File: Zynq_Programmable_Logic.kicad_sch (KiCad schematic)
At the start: 7 parts, among them Q100 T2N7002AK,LM, U1 XC7Z010-2CLG400I

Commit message: Added page '[7] 1GB DDR3L Modules'
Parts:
- renumbered D101 to D500, Q100 to Q500, R127 to R500, R104 to R501, R103 to R502, R123 to R503, U1 to U200
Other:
- company: (none) -> Designed By: Dylan Gutierrez

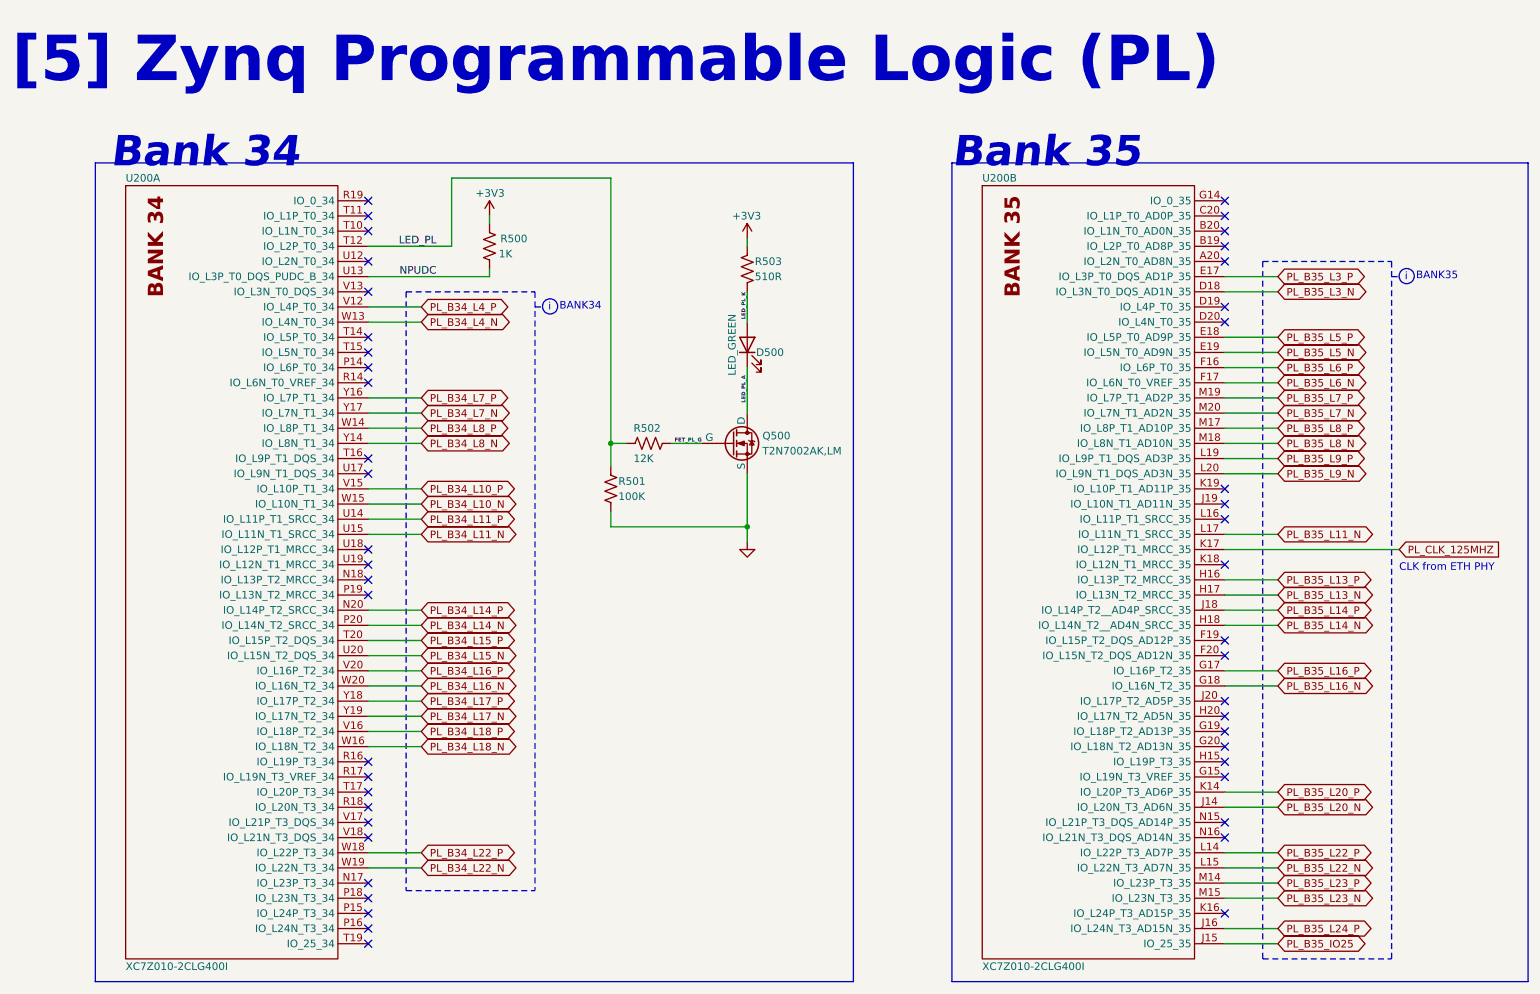
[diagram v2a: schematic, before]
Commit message: Finished first pass of schematic, needs netclass assignments and double check
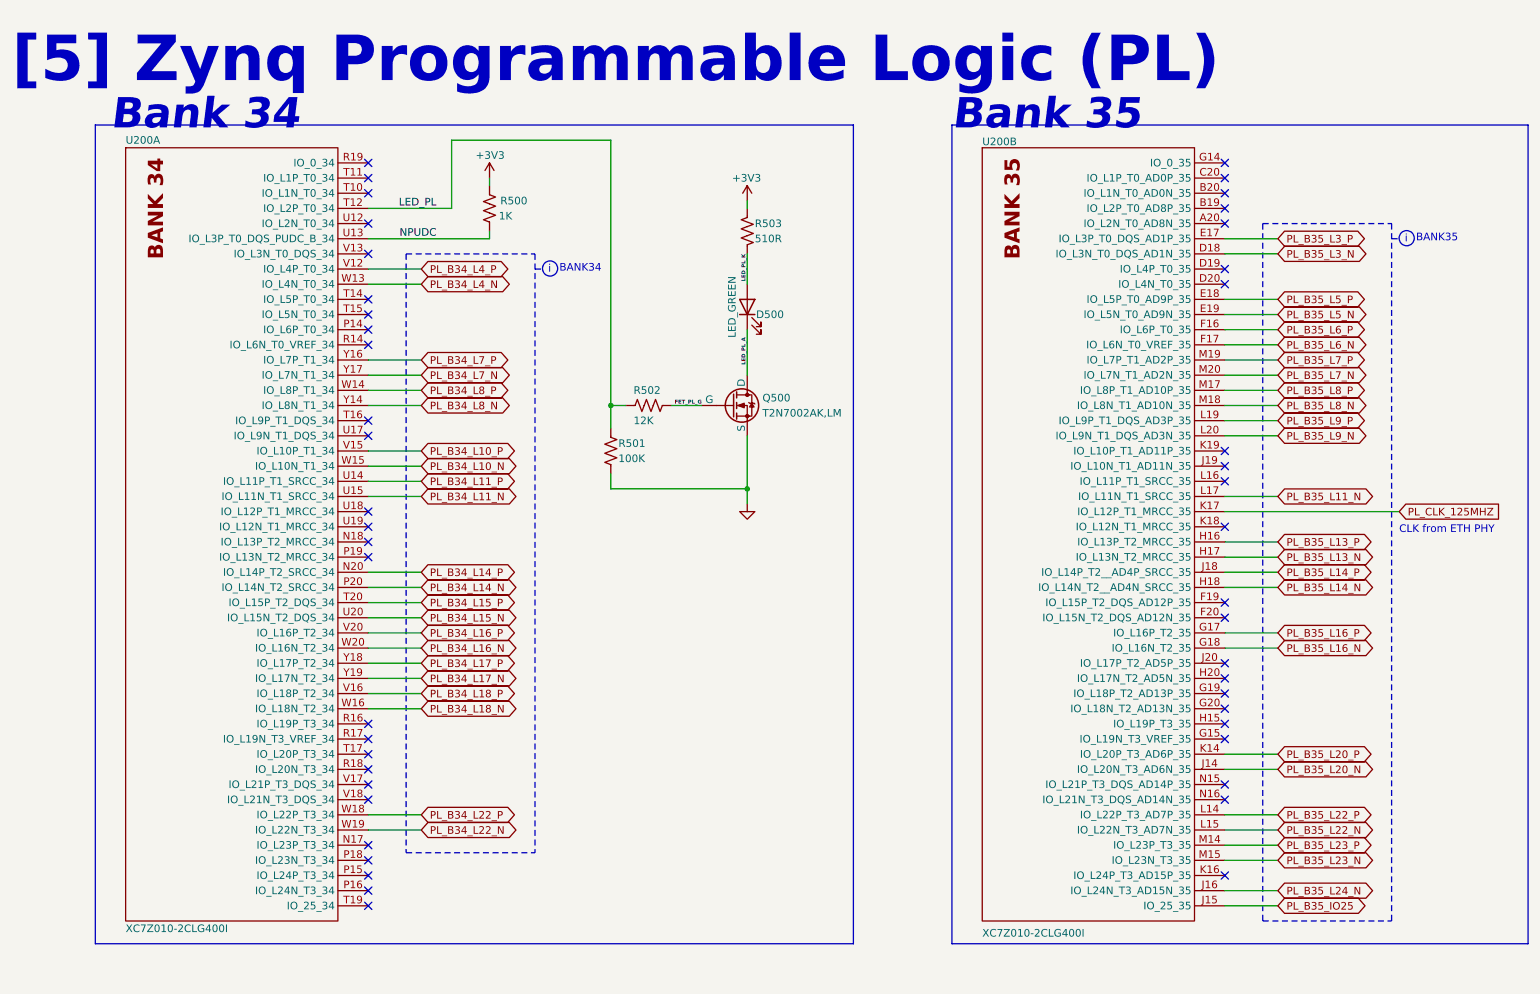
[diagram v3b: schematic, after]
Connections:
- net PL_B35_L24_P renamed PL_B35_L24_N
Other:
- moved on the sheet: D500, Q500, R500, R501, R502, R503, U200A, U200B
